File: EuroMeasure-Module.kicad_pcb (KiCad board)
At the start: 2 copper layers, 99.9 x 99.9 mm, 43 parts, among them SW201 ADR, SW202 RESET, U201 STM32G030CxT, U301 AMS1117-3.3, Y201 NX2520 16MHz

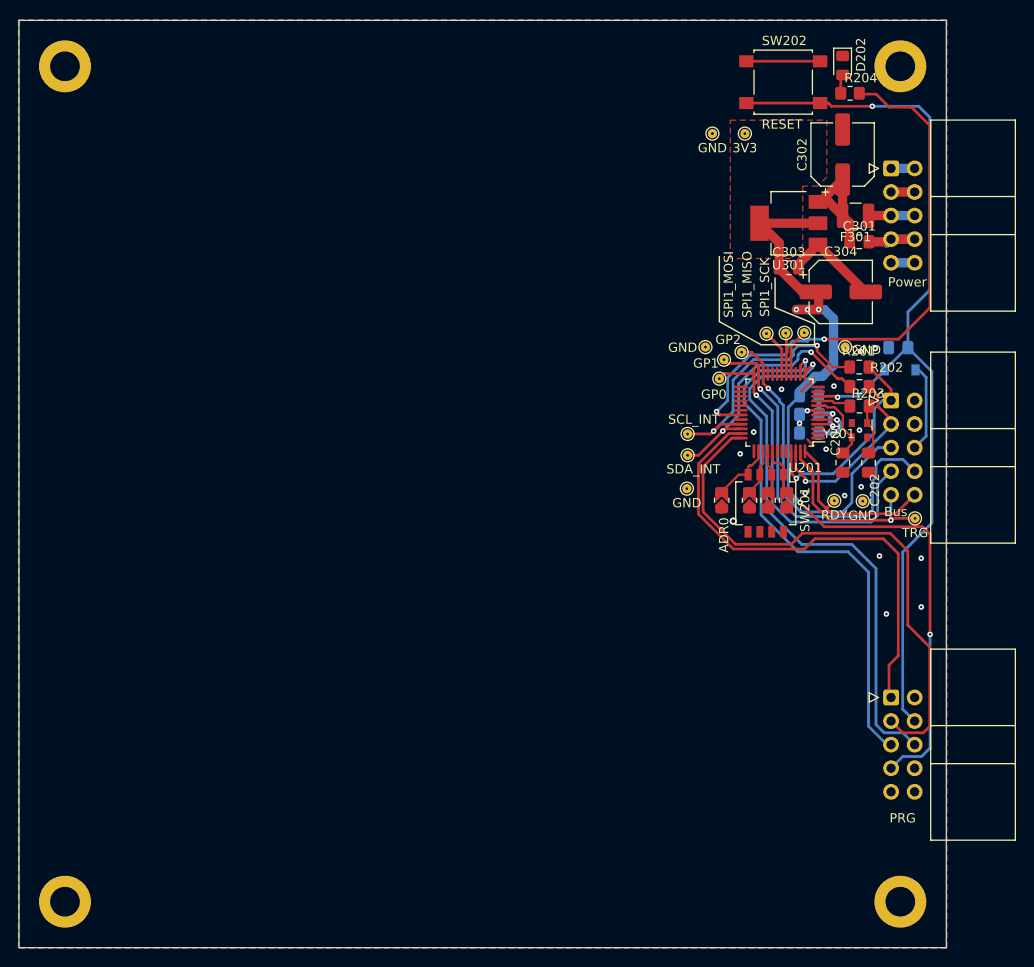
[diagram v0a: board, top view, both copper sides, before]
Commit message: Converted for use as the single EuroMeasure.sch file
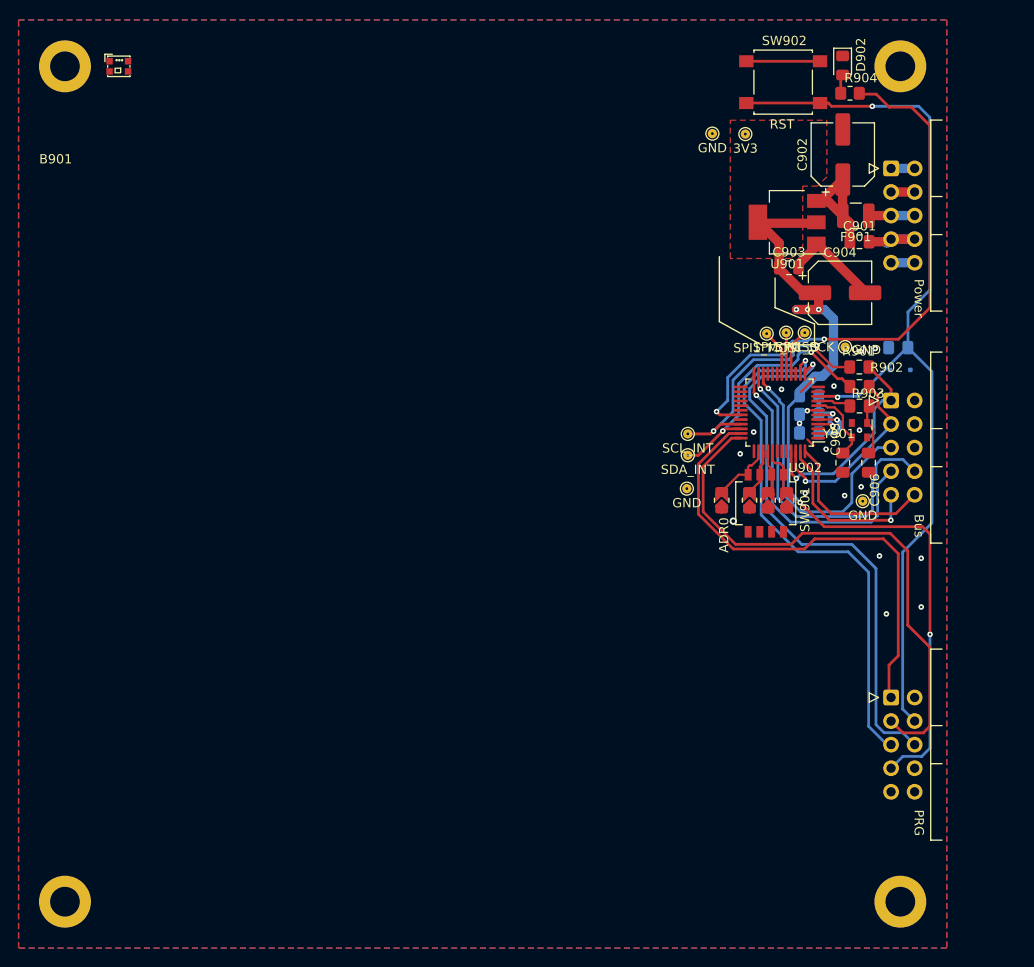
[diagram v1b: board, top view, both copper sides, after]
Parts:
- removed C301, C303: 10u, Capacitor_SMD:C_0805_2012Metric_Pad1.18x1.45mm_HandSolder
- removed C302, C304: 220u, Capacitor_SMD:CP_Elec_6.3x7.7
- removed F301: Polyfuse, Fuse:Fuse_1210_3225Metric
- removed TP204: GND, MEMS_Custom:TestPoint_Pad_D1.0mm
- removed TP206: SPI1_SCK, MEMS_Custom:TestPoint_Pad_D1.0mm
- removed TP207: SPI1_MISO, MEMS_Custom:TestPoint_Pad_D1.0mm
- removed TP208: SPI1_MOSI, MEMS_Custom:TestPoint_Pad_D1.0mm
- removed TP209: SCL_INT, MEMS_Custom:TestPoint_Pad_D1.0mm
- removed TP210: SDA_INT, MEMS_Custom:TestPoint_Pad_D1.0mm
- removed TP211: TRG, MEMS_Custom:TestPoint_Pad_D1.0mm
- removed TP212: RDY, MEMS_Custom:TestPoint_Pad_D1.0mm
- removed TP213: GP2, MEMS_Custom:TestPoint_Pad_D1.0mm
- removed TP214: GP1, MEMS_Custom:TestPoint_Pad_D1.0mm
- removed TP215: GP0, MEMS_Custom:TestPoint_Pad_D1.0mm
- removed TP301: 3V3, MEMS_Custom:TestPoint_Pad_D1.0mm
- removed U301: AMS1117-3.3, Package_TO_SOT_SMD:SOT-223-3_TabPin2
- added C901: 10u, Capacitor_SMD:C_0805_2012Metric_Pad1.18x1.45mm_HandSolder, F.Cu at (186.8, 74.0)
- added C902: 220u, Capacitor_SMD:CP_Elec_6.3x7.7, F.Cu at (185.0, 64.6)
- added C903: 10u, Capacitor_SMD:C_0805_2012Metric_Pad1.18x1.45mm_HandSolder, F.Cu at (179.2, 76.8)
- added C904: 220u, Capacitor_SMD:CP_Elec_6.3x7.7, F.Cu at (184.7, 79.5)
- added F901: Polyfuse 0.5A, Fuse:Fuse_1210_3225Metric, F.Cu at (186.4, 71.2)
- added TP905: 3V3, MEMS_Custom:TestPoint_Pad_D1.0mm, F.Cu at (174.5, 62.4)
- added TP906: SPI1_SCK, MEMS_Custom:TestPoint_Pad_D1.0mm, F.Cu at (180.9, 83.8)
- added TP907: SPI1_MISO, MEMS_Custom:TestPoint_Pad_D1.0mm, F.Cu at (178.9, 83.8)
- added TP908: SPI1_MOSI, MEMS_Custom:TestPoint_Pad_D1.0mm, F.Cu at (176.8, 83.9)
- added TP909: SCL_INT, MEMS_Custom:TestPoint_Pad_D1.0mm, F.Cu at (168.3, 94.7)
- added TP910: SDA_INT, MEMS_Custom:TestPoint_Pad_D1.0mm, F.Cu at (168.3, 97.0)
- added U901: AZ1117-3V3, Package_TO_SOT_SMD:SOT-223-3_TabPin2, F.Cu at (179.0, 71.9)
- B901: renamed from B201; footprint MEMS_Custom:EuroMeasure -> MEMS_Custom:EuroMeasureLED
- D901: renamed from D201; value 1n4148 -> 1N4148; footprint Diode_SMD:D_SOD-123 -> Diode_SMD:D_SOD-323F
- D902: renamed from D202; value LED -> RED
- L901: renamed from L201; value L_Ferrite -> Ferrite
- SW901: renamed from SW201; value ADR -> SW_DIP_x04
- SW902: renamed from SW202; value RESET -> RST
- Y901: renamed from Y201; value NX2520 16MHz -> 16MHz
- renumbered C201 to C905, C202 to C906, C203 to C907, C204 to C908, C205 to C909, JP201 to JP901, JP202 to JP902, JP203 to JP903, JP204 to JP904, R201 to R901, R202 to R902, R203 to R903, R204 to R904, TP201 to TP901, TP202 to TP902, TP203 to TP903, TP205 to TP904, U201 to U902
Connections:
- net -15V_INPUT renamed -15V
- net /EuroMeasure/GP2 renamed /EuroMeasure/~{LOCKOUT}
- net /EuroMeasure/LOCAL_RST renamed /EuroMeasure/RST_LOCAL
- net 15V_INPUT renamed +15V
- net Net-(U201-PC7) renamed /EuroMeasure/LED
- B901 pad 5: 5V_INPUT -> +5V
- B901 pad 6: 5V_INPUT -> +5V
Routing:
- net Net-(#FLG0901-pwr): track 0.00 -> 13.9 mm
- net /EuroMeasure/RST: track 9.57 -> 0.00 mm
- net +5V: track 13.9 -> 4.94 mm
- net 5V_INPUT: track 4.97 -> 0.00 mm
- net /EuroMeasure/GP1: track 40.4 -> 35.5 mm
- net /EuroMeasure/GP0: track 36.6 -> 32.7 mm
- net /EuroMeasure/~{LOCKOUT}: track 34.9 -> 30.9 mm
- net /EuroMeasure/TRG: track 20.8 -> 18.1 mm
- net /EuroMeasure/RDY: track 19.0 -> 17.7 mm
- net GND: track 36.5 -> 35.5 mm
- net /EuroMeasure/SCL_EXT: track 23.5 -> 23.0 mm
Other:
- board outline removed

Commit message: Cleaned up PCB
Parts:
- added C53: 10u, Capacitor_SMD:C_0805_2012Metric_Pad1.18x1.45mm_HandSolder, F.Cu at (115.7, 54.5)
- moved B2 3.78 mm to (100.0, 50.0)
- moved C44 3.78 mm to (190.6, 73.9)
- moved C45 3.78 mm to (188.8, 64.5)
- moved C46 3.78 mm to (183.0, 76.7)
- moved C47 3.78 mm to (188.5, 79.4)
- moved C48 3.78 mm to (188.8, 97.7)
- moved C50 3.78 mm to (194.8, 85.3)
- moved C51 3.78 mm to (185.2, 94.5)
- moved C52 3.78 mm to (185.2, 92.5)
- moved D10 3.78 mm to (188.8, 54.9)
- moved D9 3.78 mm to (195.0, 87.7)
- moved JP20 3.78 mm to (175.8, 101.8)
- moved JP21 3.78 mm to (178.8, 101.8)
- moved JP22 3.78 mm to (180.8, 101.8)
- moved JP23 3.78 mm to (182.8, 101.8)
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- renumbered B901 to B2, C901 to C44, C902 to C45, C903 to C46, C904 to C47, C905 to C48, C906 to C49, C907 to C50, C908 to C51, C909 to C52, D902 to D10, D901 to D9, F901 to F3, JP901 to JP20, JP902 to JP21, JP903 to JP22, JP904 to JP23, L901 to L1, R901 to R35, R902 to R36, R903 to R37, R904 to R38, SW901 to SW1, SW902 to SW2, TP901 to TP11, TP902 to TP12, TP903 to TP13, TP904 to TP14, TP905 to TP15, U901 to U10, U902 to U11, Y901 to Y1
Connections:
- net +15V renamed 15V_INPUT
- net -15V renamed -15V_INPUT
- net Net-(#FLG0901-pwr) renamed /EuroMeasure/5v_fused
- net Net-(#FLG0902-pwr) renamed /EuroMeasure/mcu_pwr
- net Net-(C906-Pad1) renamed /EuroMeasure/osc_mid
- net Net-(D902-A) renamed /EuroMeasure/led_r
- net Net-(U902-PF0-OSC_IN) renamed /EuroMeasure/OSC_OUT
- net Net-(U902-PF1-OSC_OUT) renamed /EuroMeasure/OSC_IN
- net Net-(U902-VREF+) renamed /EuroMeasure/vref_c
- B2 pad 28: unconnected-(B901A-NC4-Pad28) -> /EuroMeasure/NC4
- B2 pad 29: unconnected-(B901A-NC5-Pad29) -> /EuroMeasure/NC5
- B2 pad 30: unconnected-(B901A-NC6-Pad30) -> /EuroMeasure/NC6
- B2 pad 5: +5V -> 5V_INPUT
- B2 pad 6: +5V -> 5V_INPUT
- B2 pad D1: unconnected-(B901B-DO-PadD1) -> /EuroMeasure/RGB_OUT
- B2 pad D2: unconnected-(B901B-GND-PadD2) -> GND
- B2 pad D3: unconnected-(B901B-DI-PadD3) -> /EuroMeasure/RGB_LED
- B2 pad D4: unconnected-(B901B-VCC-PadD4) -> 5V_INPUT
- F3 pad 1: +5V -> 5V_INPUT
- U11 pad 11: /EuroMeasure/PA0 -> /EuroMeasure/RGB_LED
- U11 pad 2: unconnected-(U902-OSC32_IN/PC14-Pad2) -> /EuroMeasure/OSC32_IN
- U11 pad 3: unconnected-(U902-OSC32_OUT/PC15-Pad3) -> /EuroMeasure/OSC32_OUT
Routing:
- net /EuroMeasure/RGB_LED: track 0.00 -> 109.8 mm, vias 0 -> 2
- net 5V_INPUT: track 0.00 -> 96.3 mm, vias 0 -> 1
- net /EuroMeasure/RST: track 0.00 -> 9.54 mm
- net +5V: track 4.94 -> 0.00 mm
- net /EuroMeasure/RST_LOCAL: track 101.3 -> 101.8 mm
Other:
- board outline added: 100 x 100 mm

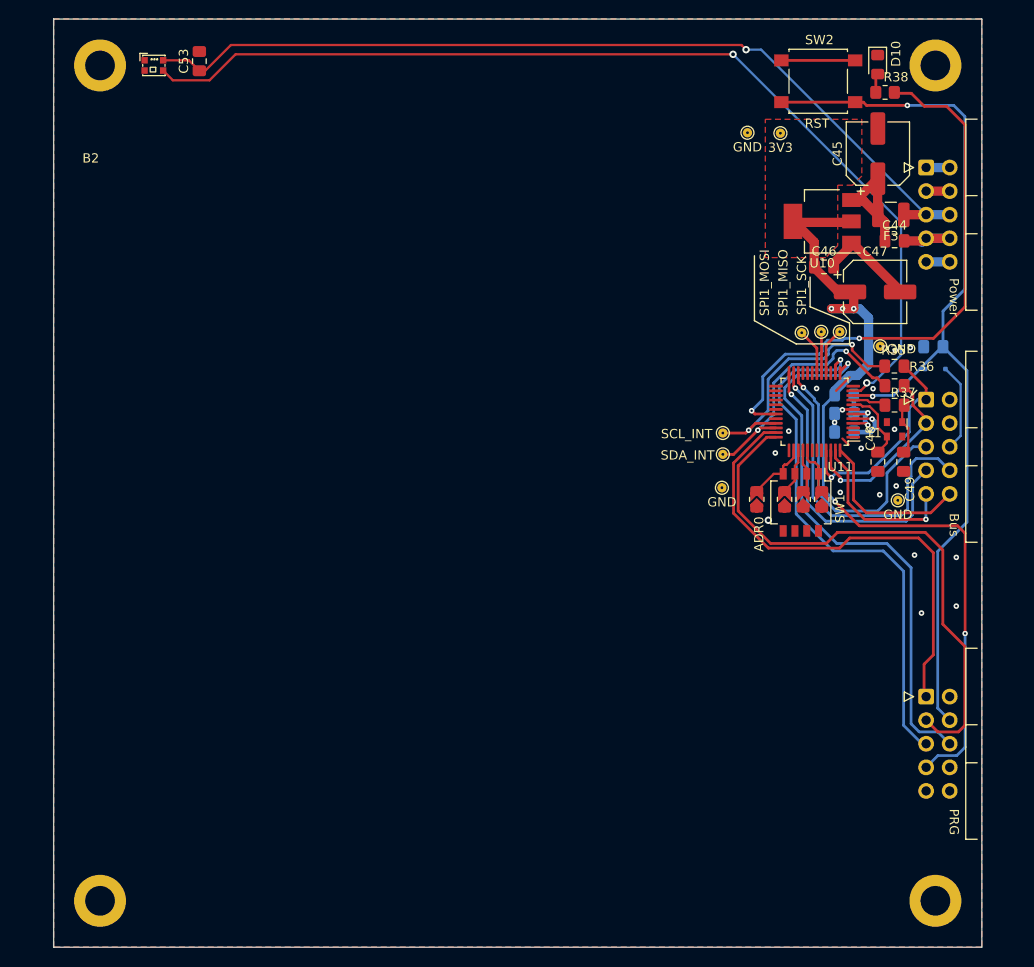
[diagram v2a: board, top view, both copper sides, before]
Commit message: Reverted duplicated components
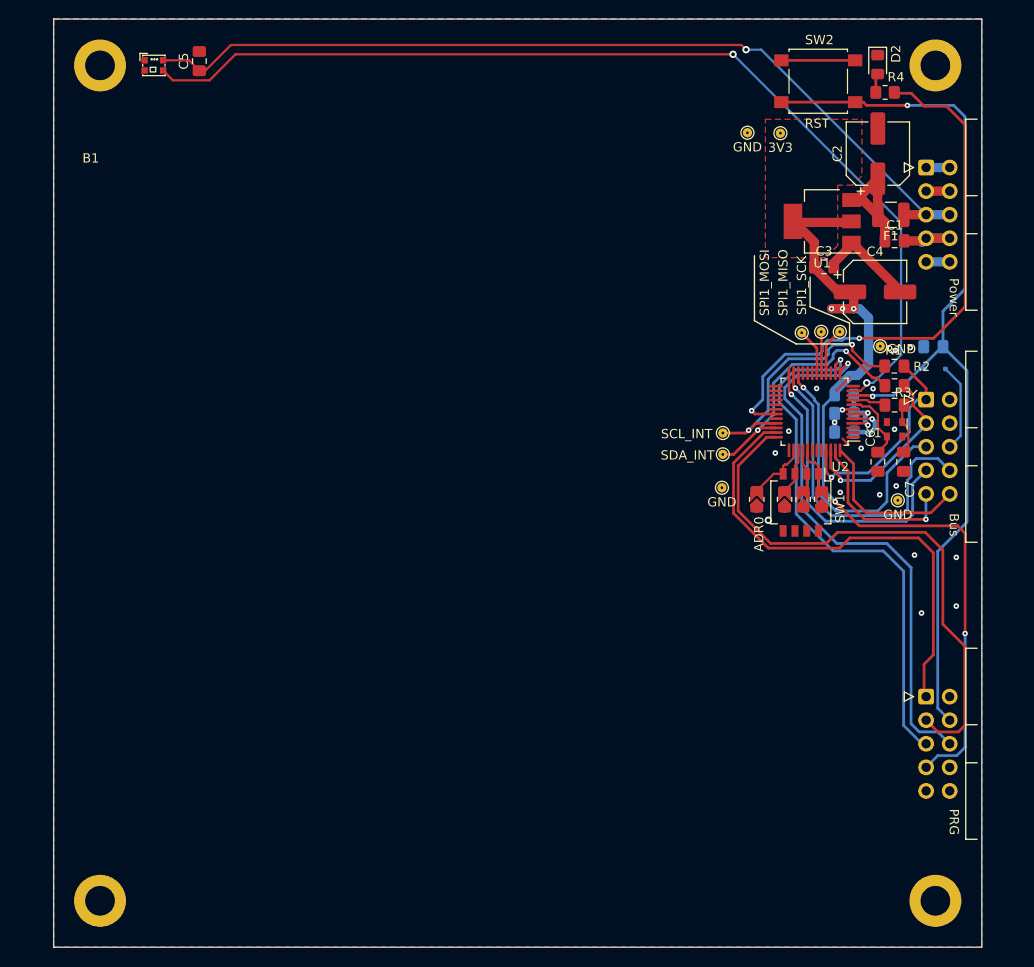
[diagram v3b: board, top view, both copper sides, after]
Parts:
- renumbered B2 to B1, C44 to C1, C52 to C10, C45 to C2, C46 to C3, C47 to C4, C53 to C5, C48 to C6, C49 to C7, C50 to C8, C51 to C9, D9 to D1, D10 to D2, F3 to F1, JP20 to JP1, JP21 to JP2, JP22 to JP3, JP23 to JP4, R35 to R1, R36 to R2, R37 to R3, R38 to R4, TP906 to TP1, TP15 to TP10, TP907 to TP2, TP908 to TP3, TP909 to TP4, TP910 to TP5, TP11 to TP6, TP12 to TP7, TP13 to TP8, TP14 to TP9, U10 to U1, U11 to U2
